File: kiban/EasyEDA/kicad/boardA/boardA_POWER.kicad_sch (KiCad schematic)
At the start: 21 parts, among them U3 LTC2954-1, U4 TPS70933, U5 TPS62933

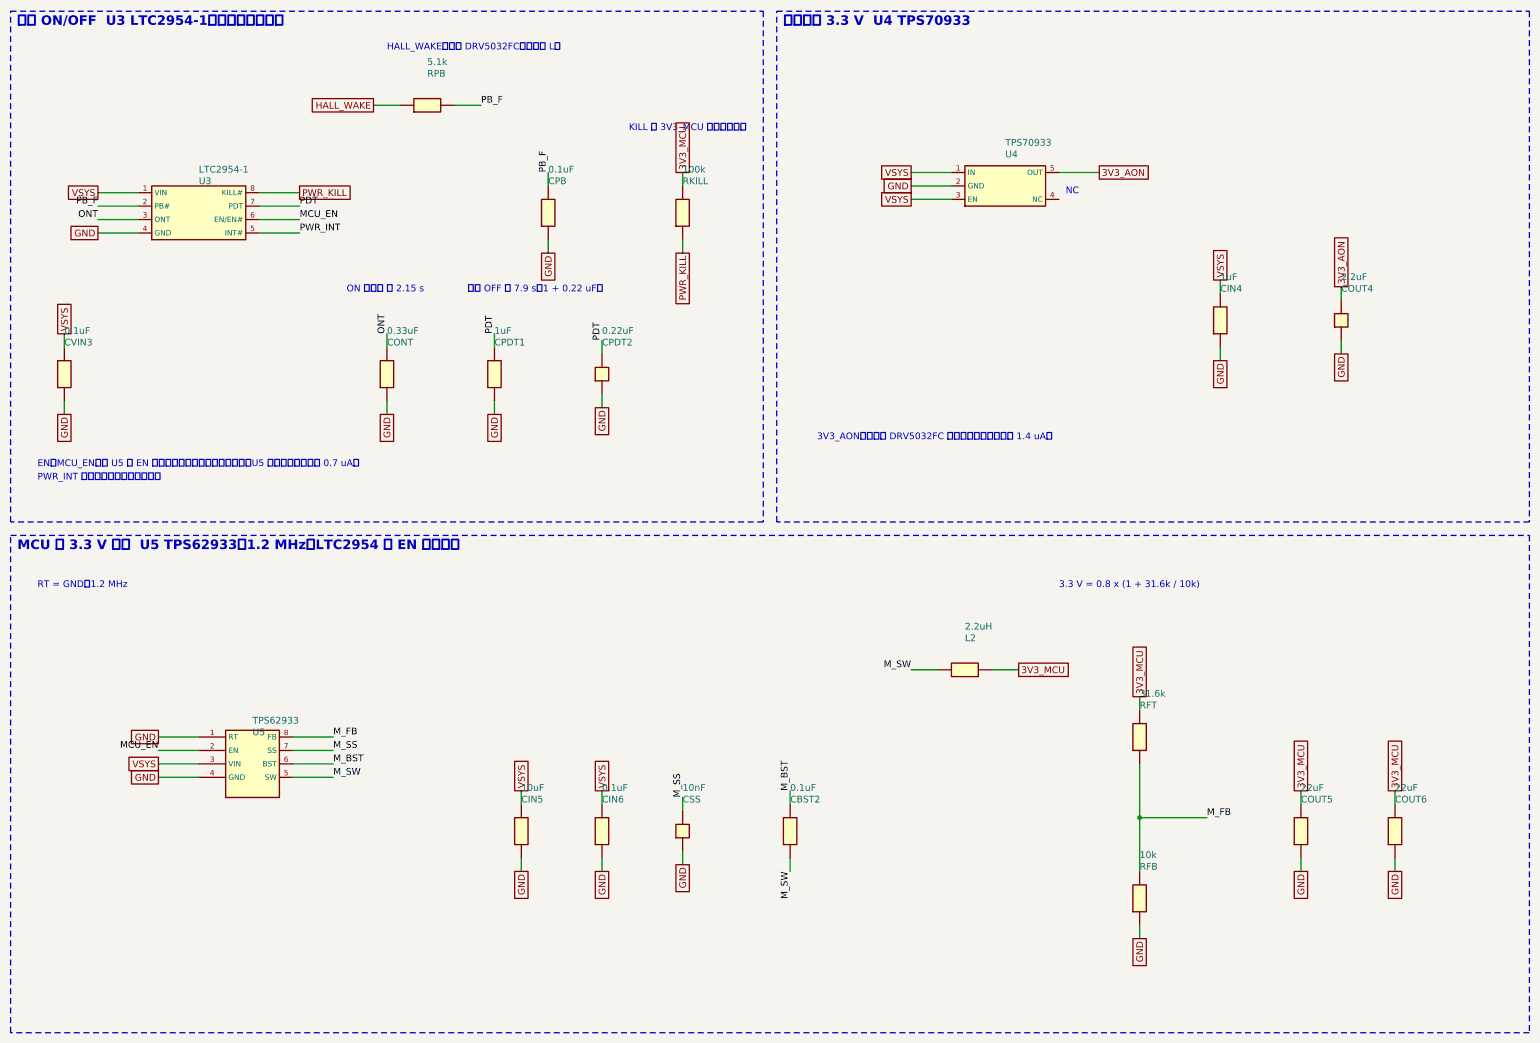
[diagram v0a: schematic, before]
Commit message: feat: KiCad 版の回路図に LCSC のシンボル・フットプリントを使う (easyeda2kicad)
- tools/kicad/lcsc_lib.py: LCSC 部品を easyeda2kicad で取得し、3D パスを直して KiCad 10 形式に更新、
  boardA / boardB に lcsc ライブラリを登録 (未取得の部品だけを、間隔を空けて取得)
- kicad_export.py: 取得したシンボルを、EasyEDA とピン位置が一致する向きで使い、フットプリントを割り当てる
  (合わない部品と未取得の部品は従来の矩形シンボル)。回転した部品の値の文字は横書きのまま
- 47 種類中 30 種類を取得 (残りは EasyEDA API の 403 で未取得)。111 部品中 82 部品が LCSC のシンボル
- kicad-cli のネットリストは基板A 23 / 基板B 43 ネットとも EasyEDA と一致
- 3D モデル (lcsc.3dshapes) と KiCad の .history/ は Git に入れない

Co-Authored-By: Claude Opus 5.5 <noreply@anthropic.com>
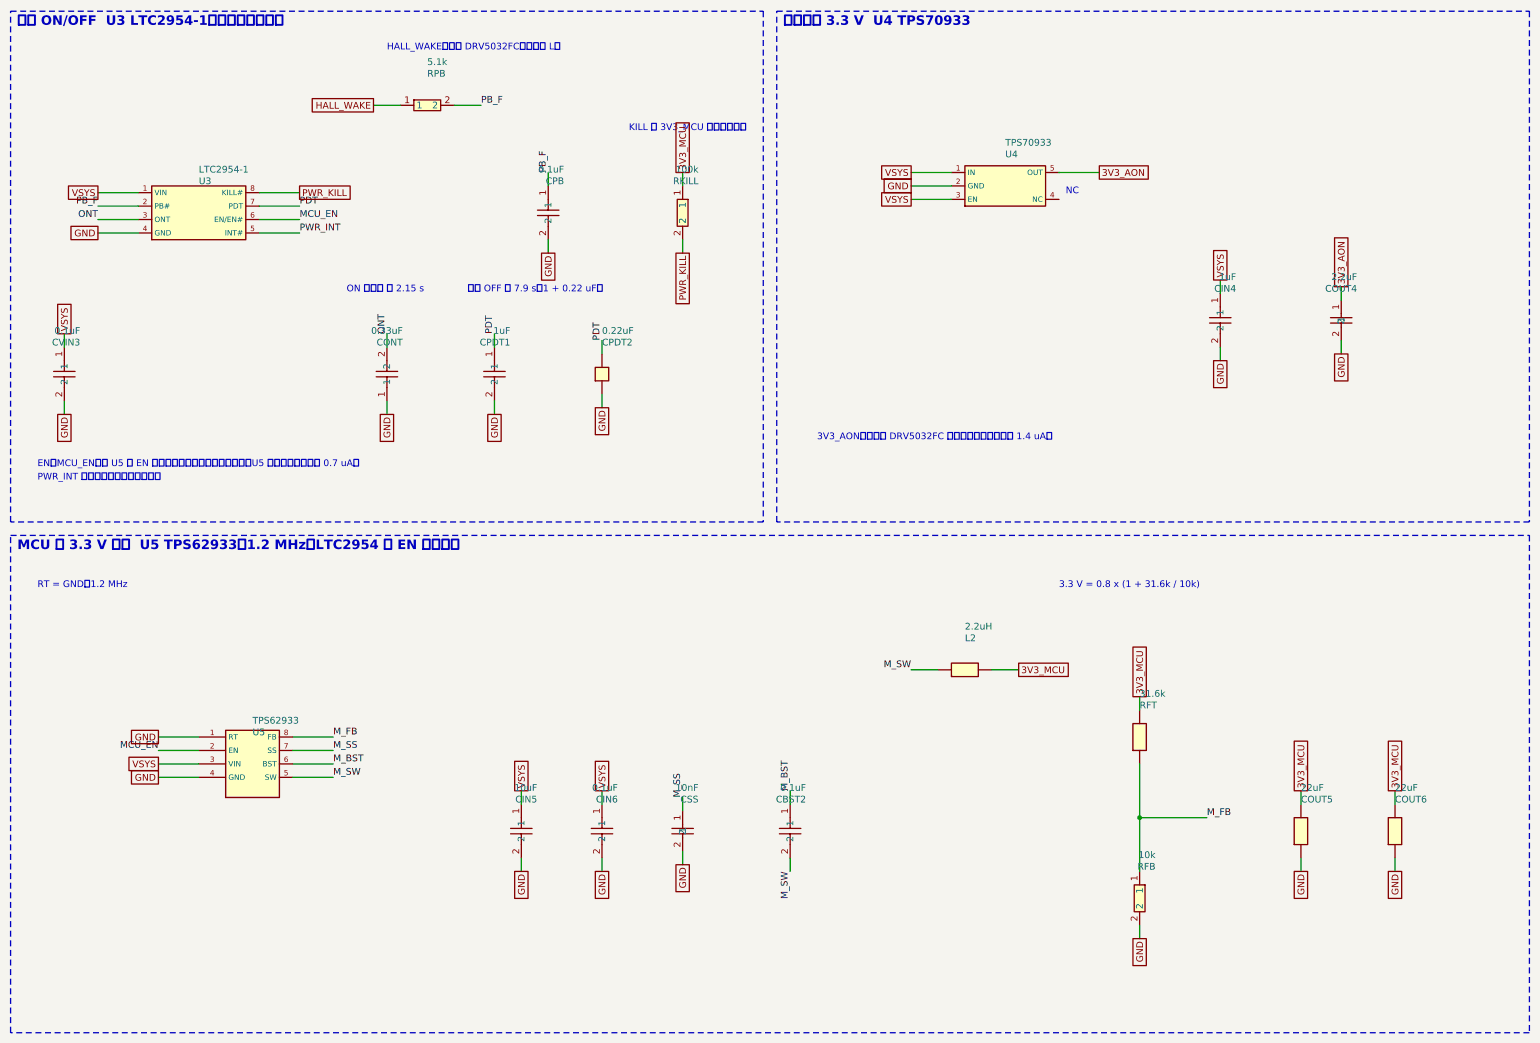
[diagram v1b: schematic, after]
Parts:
- CBST2: footprint (none) -> lcsc:C0603; symbol gen:CBST_C1591_r270 -> lcsc:CL10B104KB8NNNC
- CIN4: footprint (none) -> lcsc:C0603; symbol gen:CIN_C15849_r270 -> lcsc:CL10A105KB8NNNC
- CIN5: footprint (none) -> lcsc:C0805; symbol gen:CIN_C15850_r270 -> lcsc:CL21A106KAYNNNE
- CIN6: footprint (none) -> lcsc:C0603; symbol gen:CIN_C1591_r270 -> lcsc:CL10B104KB8NNNC
- CONT: footprint (none) -> lcsc:C0603; symbol gen:CONT_C159798_r270 -> lcsc:CL10B334KO8NNNC
- COUT4: footprint (none) -> lcsc:C0603; symbol gen:COUT_C23630_r270 -> lcsc:CL10A225KO8NNNC
- CPB: footprint (none) -> lcsc:C0603; symbol gen:CPB_C1591_r270 -> lcsc:CL10B104KB8NNNC
- CPDT1: footprint (none) -> lcsc:C0603; symbol gen:CPDT_C15849_r270 -> lcsc:CL10A105KB8NNNC
- CSS: footprint (none) -> lcsc:C0603; symbol gen:CSS_C1589_r270 -> lcsc:CL10B103KB8NNNC
- CVIN3: footprint (none) -> lcsc:C0603; symbol gen:CVIN_C1591_r270 -> lcsc:CL10B104KB8NNNC
- RFB: footprint (none) -> lcsc:R0603; symbol gen:RFB_C25804_r270 -> lcsc:0603WAF1002T5E
- RKILL: footprint (none) -> lcsc:R0603; symbol gen:RKILL_C25803_r270 -> lcsc:0603WAF1003T5E
- RPB: footprint (none) -> lcsc:R0603; symbol gen:RPB_C23186_r0 -> lcsc:0603WAF5101T5E
